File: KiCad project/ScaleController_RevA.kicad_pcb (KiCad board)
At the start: 4 copper layers, 89.9 x 52.8 mm, 57 parts, among them J1 USB_C_Receptacle, J3 MTMM-103-03-T-S-150, J5 MTMM-103-03-T-S-150, J6 Conn_01x05, J7 MTMM-103-03-T-S-150, J8 MTMM-103-03-T-S-150, J9 Conn_01x04_Socket, Q2 BC817, Q3 BC817, SW1 1101NE, SW2 1101NE, U2 LM1117MPX-3.3_NOPB, U3 ESP32-C3-WROOM-02-H4, U4 CP2102N-A02-GQFN20, U5 USBLC6-2SC6, U6 HX711

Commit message: Swap E+/E- labels so E+ is the 3.3V-side excitation again
Pure rename: the four E+ and four E- labels on the HX711 sheet exchanged,
and the two net names on the board exchanged to match. No wire, pad or
track changed. Netlist: E+ = J3.1 J5.3 J7.1 J8.3 NT2.2 (3.3V tie);
E- = J3.3 J5.1 J7.3 J8.1 NT3.2 (GND tie). ERC 0 errors; DRC 0 unrouted,
4 warnings; every pad net on the board matches the schematic.

Co-Authored-By: Claude Fable 5.1 <noreply@anthropic.com>
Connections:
- J3 pad 1: /HX711_LoadCell_Summing/E- -> /HX711_LoadCell_Summing/E+
- J3 pad 3: /HX711_LoadCell_Summing/E+ -> /HX711_LoadCell_Summing/E-
- J5 pad 1: /HX711_LoadCell_Summing/E+ -> /HX711_LoadCell_Summing/E-
- J5 pad 3: /HX711_LoadCell_Summing/E- -> /HX711_LoadCell_Summing/E+
- J7 pad 1: /HX711_LoadCell_Summing/E- -> /HX711_LoadCell_Summing/E+
- J7 pad 3: /HX711_LoadCell_Summing/E+ -> /HX711_LoadCell_Summing/E-
- J8 pad 1: /HX711_LoadCell_Summing/E+ -> /HX711_LoadCell_Summing/E-
- J8 pad 3: /HX711_LoadCell_Summing/E- -> /HX711_LoadCell_Summing/E+
- NT2 pad 2: /HX711_LoadCell_Summing/E- -> /HX711_LoadCell_Summing/E+
- NT3 pad 2: /HX711_LoadCell_Summing/E+ -> /HX711_LoadCell_Summing/E-
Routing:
- net /HX711_LoadCell_Summing/E-: track 26.7 -> 24.6 mm
- net /HX711_LoadCell_Summing/E+: track 24.6 -> 26.7 mm
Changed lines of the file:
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@@
 	(net 51 "unconnected-(J1-CC1-PadA5)")
 	(net 52 "/HX711_LoadCell_Summing/S_PLUS_GRP")
-	(net 53 "/HX711_LoadCell_Summing/E-")
-	(net 54 "/HX711_LoadCell_Summing/E+")
+	(net 53 "/HX711_LoadCell_Summing/E+")
+	(net 54 "/HX711_LoadCell_Summing/E-")
 	(net 55 "/HX711_LoadCell_Summing/S_MINUS_GRP")
 	(net 56 "/ESP32-C3-02/DOUT")
@@
 			(remove_unused_layers no)
 			(roundrect_rratio 0.208333)
-			(net 54 "/HX711_LoadCell_Summing/E+")
+			(net 54 "/HX711_LoadCell_Summing/E-")
 		)
 		(pad "2" thru_hole oval
@@
 			(layers "*.Cu" "*.Mask")
 			(remove_unused_layers no)
-			(net 53 "/HX711_LoadCell_Summing/E-")
+			(net 53 "/HX711_LoadCell_Summing/E+")
 		)
 		(embedded_fonts no)
@@
 			(remove_unused_layers no)
 			(roundrect_rratio 0.208333)
-			(net 53 "/HX711_LoadCell_Summing/E-")
+			(net 53 "/HX711_LoadCell_Summing/E+")
 		)
 		(pad "2" thru_hole oval
@@
 			(layers "*.Cu" "*.Mask")
 			(remove_unused_layers no)
-			(net 54 "/HX711_LoadCell_Summing/E+")
+			(net 54 "/HX711_LoadCell_Summing/E-")
 		)
 		(embedded_fonts no)
@@
 			(remove_unused_layers no)
 			(roundrect_rratio 0.208333)
-			(net 53 "/HX711_LoadCell_Summing/E-")
+			(net 53 "/HX711_LoadCell_Summing/E+")
 		)
 		(pad "2" thru_hole oval
@@
 			(layers "*.Cu" "*.Mask")
 			(remove_unused_layers no)
-			(net 54 "/HX711_LoadCell_Summing/E+")
+			(net 54 "/HX711_LoadCell_Summing/E-")
 		)
 		(embedded_fonts no)
@@
 			(size 2 2)
 			(layers "F.Cu")
-			(net 53 "/HX711_LoadCell_Summing/E-")
+			(net 53 "/HX711_LoadCell_Summing/E+")
 			(pinfunction "2")
 			(pintype "passive")
@@
 			(size 2 2)
 			(layers "F.Cu")
-			(net 54 "/HX711_LoadCell_Summing/E+")
+			(net 54 "/HX711_LoadCell_Summing/E-")
 			(pinfunction "2")
 			(pintype "passive")
@@
 			(remove_unused_layers no)
 			(roundrect_rratio 0.208333)
-			(net 54 "/HX711_LoadCell_Summing/E+")
+			(net 54 "/HX711_LoadCell_Summing/E-")
 		)
 		(pad "2" thru_hole oval
@@
 			(layers "*.Cu" "*.Mask")
 			(remove_unused_layers no)
-			(net 53 "/HX711_LoadCell_Summing/E-")
+			(net 53 "/HX711_LoadCell_Summing/E+")
 		)
 		(embedded_fonts no)

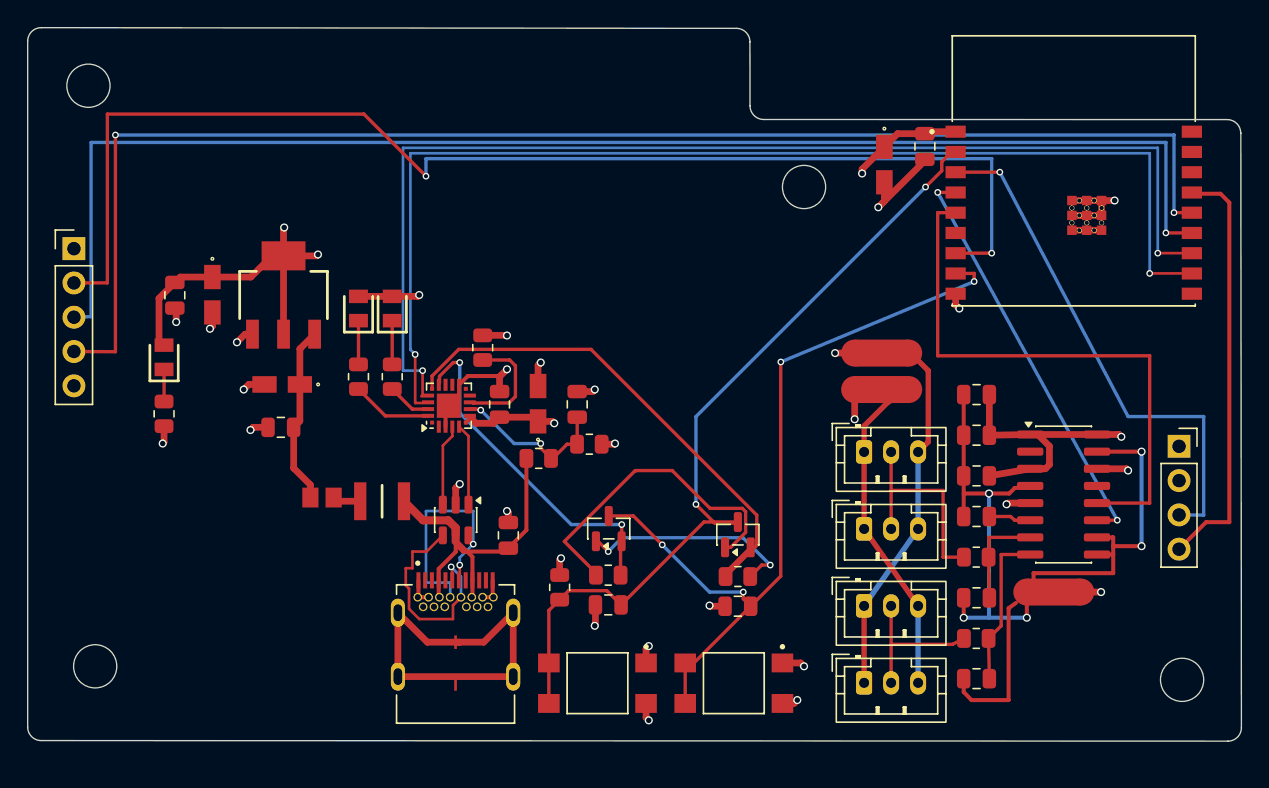
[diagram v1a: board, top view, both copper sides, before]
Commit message: Silkscreen labels
Load-cell sockets LC1-LC4 with wiring legend (1=WHT 2=RED 3=BLK, any
cell to any socket), RESET and BOOT/TARE buttons, J6 and J9 pin names,
PWR/TX/RX LEDs, board name and date. 23 board-level texts, F.SilkS,
0.75-1.5 mm height, 0.15 mm stroke. Connector reference designators
hidden in favour of the LC labels.

DRC: 0 unrouted, 4 warnings (J1/U3 lib mismatch, U3 outline over the
antenna notch).

Co-Authored-By: Claude Fable 5.1 <noreply@anthropic.com>
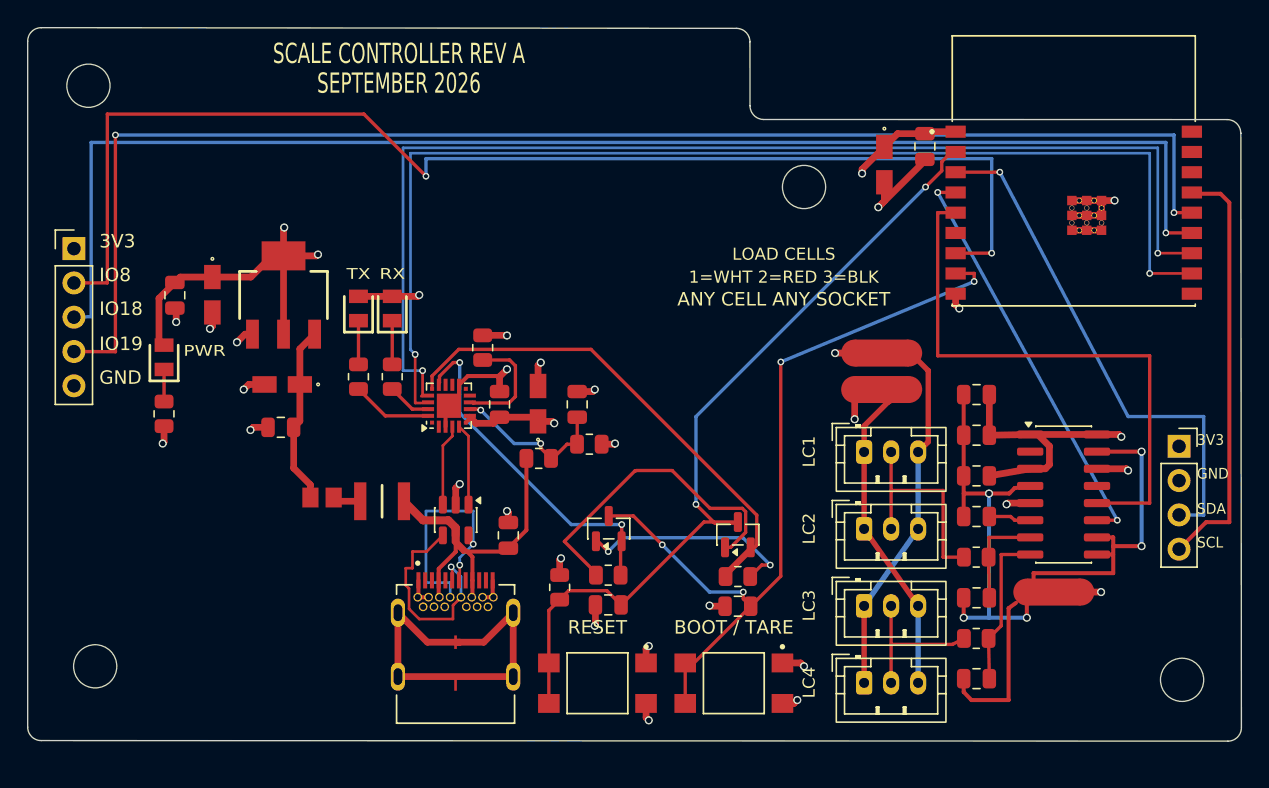
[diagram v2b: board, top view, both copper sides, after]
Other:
- board text added: "1=WHT 2=RED 3=BLK"
- board text added: "3V3"
- board text added: "ANY CELL ANY SOCKET"
- board text added: "BOOT / TARE"
- board text added: "GND"
- board text added: "IO18"
- board text added: "IO19"
- board text added: "IO8"
- board text added: "LC1"
- board text added: "LC2"
- board text added: "LC3"
- board text added: "LC4"
- board text added: "LOAD CELLS"
- board text added: "PWR"
- board text added: "RESET"
- board text added: "RX"
- board text added: "SCALE CONTROLLER REV A"
- board text added: "SCL"
- board text added: "SDA"
- board text added: "SEPTEMBER 2026"
- board text added: "TX"

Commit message: DFM pass for PCBWay: USB-C rework, 0.15 mm via rings, pad and rule fixes
USB corner rebuilt around the HRO TYPE-C-31-M-12: J1 placed with the
pad row 6.4 mm from the board edge per datasheet; D+/D- from the A pins
straight to the ESD array with the B6 join as an inner loop and the B7
join hopping the bottom layer; VBUS pins joined by an inner loop and
brought out through vias to U5, F1, C1 and R12; CC1/CC2 to R1/R2 (5.1k)
with GND vias; GND pins tied to the shell legs. Pad nets re-synced from
the schematic (14 corrected after the earlier shorted update).

DFM: all vias now 0.6/0.3 (0.15 mm ring; one 0.55/0.3 at U4 pad 8 where
the RST/C10 gap allows no more); ESP32 module ground-grid PTH pads 0.4 ->
0.6; copper-to-edge rule 0.3; net-class vias 0.6/0.3. U4 pin 12 grounds
into the centre pad so RST runs straight to R11. Top-edge bus lanes
re-spaced for the larger GPIO19 via; Q2/Q3 base tracks and the Net-(U4-
VBUS) via nudged clear of enlarged vias.

Verified on a fill-stripped copy: 0 violations, 0 unrouted. Fills stale
in this commit; refill in GUI.

Co-Authored-By: Claude Fable 5.1 <noreply@anthropic.com>
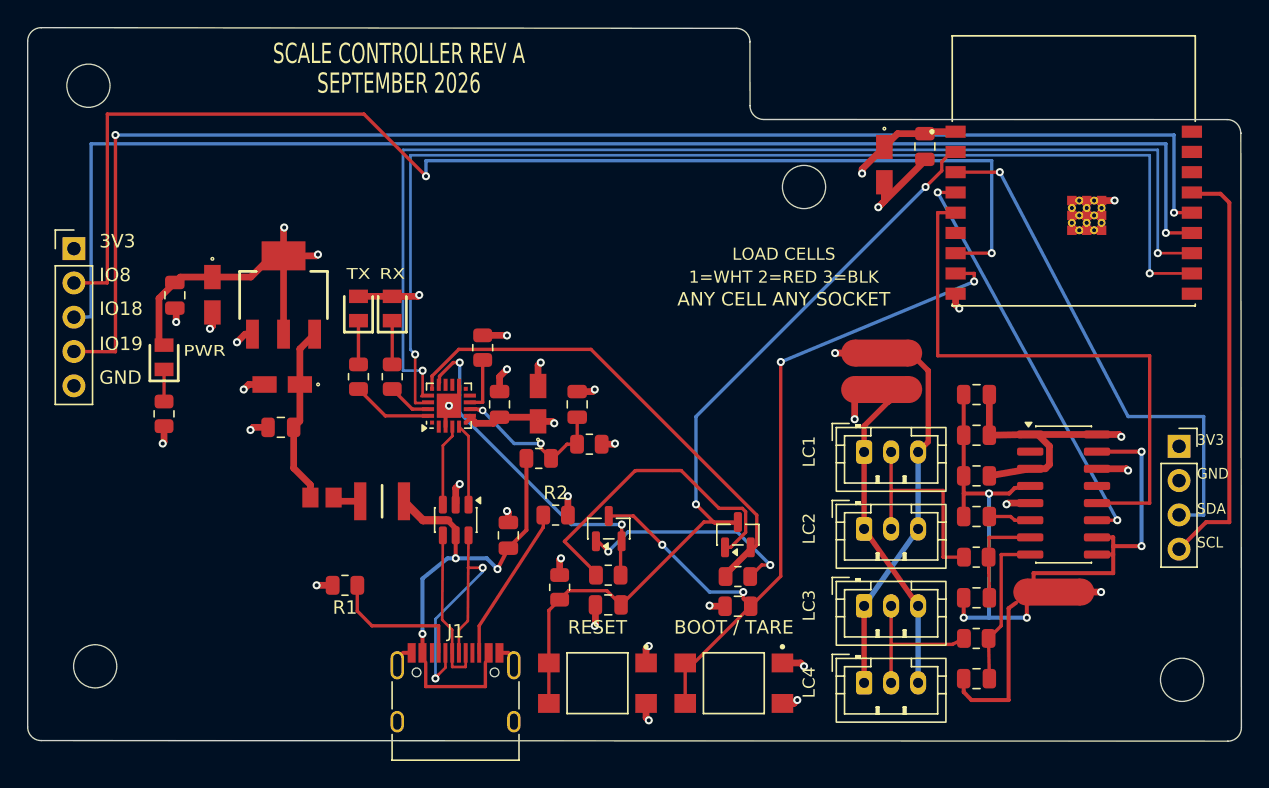
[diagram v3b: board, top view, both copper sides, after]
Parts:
- added R1: 5.1k, Resistor_SMD:R_0805_2012Metric, F.Cu at (135.0, 113.5)
- added R2: 5.1k, Resistor_SMD:R_0805_2012Metric, F.Cu at (150.6, 108.3)
- J1: value USB_C_Receptacle -> USB_C_Receptacle_USB2.0_16P; footprint Footprints:BELFUSE_SS-52400-002 -> Connector_USB:USB_C_Receptacle_HRO_TYPE-C-31-M-12
- moved J1 2.29 mm to (143.2, 122.5)
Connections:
- J1 pad A5: unconnected-(J1-CC1-PadA5) -> Net-(J1-CC1)
- J1 pad B5: unconnected-(J1-CC2-PadB5) -> Net-(J1-CC2)
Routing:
- net GND: track 89.0 -> 60.1 mm, vias 25 -> 28
- net Net-(J1-CC2): track 0.00 -> 11.6 mm
- net Net-(J1-CC1): track 0.00 -> 10.4 mm
- net /VBUS: track 26.7 -> 35.8 mm, vias 0 -> 3
- net Net-(U4-~{TXT}/GPIO.2): track 0.00 -> 5.97 mm
- net Net-(U4-~{TXT}/GPIO.2): track 5.97 -> 0.00 mm
- net /USB_DP: track 16.6 -> 10.7 mm, vias 1 -> 0
- net Net-(U4-~{RST}): track 8.28 -> 4.09 mm
- net /USB_DN: track 17.7 -> 21.9 mm
- net Net-(U4-~{RXT}/GPIO.3): track 0.00 -> 3.27 mm
- net Net-(U4-~{RXT}/GPIO.3): track 3.27 -> 0.00 mm
- net /ESP32-C3-02/GPIO18: track 101.6 -> 100.6 mm
- net Net-(U4-VBUS): track 11.9 -> 12.7 mm

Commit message: Refill zones after DFM pass; GCT USB4105 3D model as stand-in for J1
The KiCad library footprint for the HRO TYPE-C-31-M-12 references a 3D
model that was never published; the GCT USB4105 model (same 16-pin
top-mount form factor and shell-leg positions) is used for rendering.
DRC: 0 unrouted, 3 warnings (U3 lib mismatch, 2 module outline vs edge).

Co-Authored-By: Claude Fable 5.1 <noreply@anthropic.com>
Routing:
- net Net-(U4-~{TXT}/GPIO.2): track 5.97 -> 0.00 mm
- net Net-(U4-~{TXT}/GPIO.2): track 0.00 -> 5.97 mm
- net GND: track 60.1 -> 56.2 mm
- net /VBUS: track 35.8 -> 39.6 mm
- net Net-(U4-~{RXT}/GPIO.3): track 3.27 -> 0.00 mm
- net Net-(U4-~{RXT}/GPIO.3): track 0.00 -> 3.27 mm

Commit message: Add mechanical placeholder for the 1.3in OLED module plugged into J9
DISP1: pad-less footprint (board-only, excluded from BOM and placement)
with a hand-built VRML model of a nominal 4-pin 1.3in I2C OLED module
(PCB 35.4 x 33.5 mm, glass 35 x 20, corner holes) standing in J9's
vertical socket. For fit and enclosure planning only; nothing electrical
changes. Footprint stored in the project library so DRC has a matching
library copy. DRC: 0 unrouted, 5 benign warnings.

Co-Authored-By: Claude Fable 5.1 <noreply@anthropic.com>
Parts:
- added DISP1: OLED 1.3in module (fit check only), Footprints:OLED_1.3in_I2C_module_plugged, F.Cu at (196.8, 103.2)
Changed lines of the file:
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@@
+		)
+	)
+	(footprint "Footprints:OLED_1.3in_I2C_module_plugged"
+		(layer "F.Cu")
+		(at 196.775 103.205)
+		(descr "Mechanical placeholder: 1.3in I2C OLED module plugged into J9 (nominal 35.4 x 33.5 mm)")
+		(property "Reference" "DISP1"
+			(at -3 -3.81 90)
+			(layer "F.Fab")
+			(effects (font (size 0.8 0.8) (thickness 0.12)))
+		)
+		(property "Value" "OLED 1.3in module (fit check only)"
+			(at 3 -3.81 90)
+			(layer "F.Fab")
+			(hide yes)
+			(effects (font (size 0.8 0.8) (thickness 0.12)))
+		)
+		(attr board_only exclude_from_pos_files exclude_from_bom)
+		(fp_rect (start -0.6 -21.51) (end 0.6 13.89) (stroke (width 0.1) (type default)) (fill no) (layer "F.Fab"))
+		(fp_text user "OLED module plugged into J9 (mechanical)" (at 5.5 -3.81 90) (layer "Cmts.User") (effects (font (size 0.8 0.8) (thickness 0.12))))
+		(model "${KIPRJMOD}/Libraries/3D models/OLED_1.3in_I2C_module_plugged.wrl"
+			(offset (xyz 0 0 0))
+			(scale (xyz 1 1 1))
+			(rotate (xyz 0 0 0))
 		)
 	)

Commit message: OLED header J9 on the back side with the module's pin order
J9 rewired to 1=GND 2=3V3 3=SCL 4=SDA (the order on the 0.96in Hosyond
I2C module) and flipped to the bottom side, so the module plugs in from
below and lies flat under the board, clear of the load-cell sockets.
SCL/SDA tails re-routed to the swapped pads; 3V3/GND land on the planes.
J9 labels reordered on top and duplicated mirrored on the back. The
DISP1 placeholder now models the 0.96in module (27 x 27.5 mm) under the
board, replacing the 1.3in upright placeholder.

Fills stale in this commit (refill in GUI). Enclosure note: standoffs
under the board need >= 14 mm for the module.

Co-Authored-By: Claude Fable 5.1 <noreply@anthropic.com>
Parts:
- DISP1: value OLED 1.3in module (fit check only) -> OLED 0.96in module (fit check only); footprint Footprints:OLED_1.3in_I2C_module_plugged -> Footprints:OLED_0.96in_I2C_module_under
- J9: moved to B.Cu
- turned J9 to 180 degrees
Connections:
- J9 pad 1: 3.3V -> GND
- J9 pad 2: GND -> 3.3V
- J9 pad 3: /ESP32-C3-02/SDA -> /ESP32-C3-02/SCL
- J9 pad 4: /ESP32-C3-02/SCL -> /ESP32-C3-02/SDA
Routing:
- net /ESP32-C3-02/SDA: track 37.7 -> 40.2 mm
- net /ESP32-C3-02/SCL: track 30.9 -> 29.5 mm
